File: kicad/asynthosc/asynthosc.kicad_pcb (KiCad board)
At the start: 4 copper layers, 69 x 106 mm, 218 parts, among them J1 USB_B_Micro, J10 AudioJack3, J11 AudioJack3, J12 RJ45_LED_Shielded, J13 AudioJack3, J14 AudioJack3, J2 Conn_02x05_Odd_Even, J3 Conn_ARM_SWD_TagConnect_TC203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, J4 Conn_02x07_Odd_Even, J5 Conn_02x04_Odd_Even, J6 AudioJack3, J7 AudioJack3, J8 AudioJack3, J9 AudioJack3, Q1 Q_NPN_BEC, Q2 Q_NPN_BEC, SW1 SW_Push, SW10 SW_MEC_5G_LED, SW11 SW_DIP_x04, SW2 SW_MEC_5G_LED, SW6 SW_MEC_5G_LED, SW8 RotaryEncoder, SW9 SW_MEC_5G_LED, U1 LM1117S-3.3, U10 LAN8742A, U11 USBLC6-2P6, U12 H11L1, U2 LMR62421XMF, U3 USBLC6-2SC6, U4 LM1117S-5.0, U5 Si1869DH, U6 STM32F723VETx, U7 W25Q32JVSS, U8 MCP6004, U9 MCP6004, Y1 8MHz, 8pF, Y2 25MHZ,20PF,30PPM

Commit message: pcb: place and change some components for easier routing
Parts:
- removed D10, D11, D12, D13, D14, D16, D17, D9: D_Schottky_1N5817, Diode_SMD:D_SOD-123
- removed SW11: SW_DIP_x04, Button_Switch_SMD:SW_DIP_SPSTx04_Slide_6.7x11.72mm_W8.61mm_P2.54mm_LowProfile
- removed TP1, TP4: TestPoint, TestPoint:TestPoint_Pad_D1.0mm
- added D22: D_Schottky_Dual_SD103ASDM, Package_TO_SOT_SMD:SOT-23-6, F.Cu at (99.1, 115.5)
- added D24: D_Schottky_Dual_SD103ASDM, Package_TO_SOT_SMD:SOT-23-6, F.Cu at (142.4, 116.3)
- added SW3: SW_DIP_x02, Button_Switch_SMD:SW_DIP_SPSTx02_Slide_9.78x7.26mm_W8.61mm_P2.54mm, F.Cu at (92.5, 134.0)
- added SW4: SW_DIP_x02, Button_Switch_SMD:SW_DIP_SPSTx02_Slide_9.78x7.26mm_W8.61mm_P2.54mm, F.Cu at (148.5, 134.0)
- moved R32 133.4 mm to (89.0, 119.1), turned to 180 degrees
- moved C34 132.3 mm to (88.5, 120.5), turned to 180 degrees
- moved R30 130.3 mm to (92.0, 122.0)
- moved R31 127.7 mm to (93.0, 122.0), turned to -90 degrees
- moved C31 100.3 mm to (118.5, 127.0), turned to 90 degrees
- moved R23 98.6 mm to (115.5, 133.0)
- moved R20 97.8 mm to (117.0, 130.5), turned to 180 degrees
- moved C32 97.8 mm to (118.0, 133.0), turned to 180 degrees
- moved R22 96.2 mm to (118.0, 131.5)
- moved R21 95.8 mm to (118.5, 130.0), turned to -90 degrees
- moved R37 84.1 mm to (94.0, 122.0), turned to -90 degrees
- moved R36 82.9 mm to (95.0, 122.0), turned to -90 degrees
- moved R38 81.9 mm to (97.0, 119.0)
- moved C35 80.2 mm to (97.5, 120.5)
- moved U9 65.0 mm to (148.0, 116.5), turned to 90 degrees
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- renumbered JP11 to JP10, JP4 to JP3, JP5 to JP4, JP6 to JP5, JP7 to JP6, JP8 to JP7, JP9 to JP8, JP10 to JP9, SW6 to SW5, SW8 to SW6, SW9 to SW7, SW10 to SW8
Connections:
- C32 pad 1: Net-(U9D-+) -> Net-(U8C-+)
- C33 pad 1: unconnected-(C33-Pad1) -> GND
- C36 pad 2: Net-(U8C--) -> Net-(U9A--)
- C37 pad 1: unconnected-(C37-Pad1) -> GND
- C50 pad 2: Net-(U8D--) -> Net-(U9B--)
- JP8 pad 1: Net-(JP9-A) -> Net-(JP8-A)
- R21 pad 1: Net-(U9D-+) -> Net-(U8C-+)
- R22 pad 2: Net-(U9D-+) -> Net-(U8C-+)
- R41 pad 1: Net-(U8C--) -> Net-(U9A--)
- R42 pad 1: Net-(U8C-+) -> Net-(U9A-+)
- R43 pad 1: Net-(U8C-+) -> Net-(U9A-+)
- R44 pad 2: Net-(U8C--) -> Net-(U9A--)
- R72 pad 1: Net-(U8D--) -> Net-(U9B--)
- R73 pad 1: Net-(U8D-+) -> Net-(U9B-+)
- R74 pad 1: Net-(U8D-+) -> Net-(U9B-+)
- R75 pad 2: Net-(U8D--) -> Net-(U9B--)
- U10 pad 15: Net-(JP9-A) -> Net-(JP8-A)
- U8 pad 12: Net-(U8D-+) -> (no net)
- U8 pad 13: Net-(U8D--) -> (no net)
- U8 pad 14: /Analog_in/CVIN3 -> (no net)
- U8 pad 8: /Analog_in/CVIN2 -> Net-(C32-Pad2)
- U8 pad 9: Net-(U8C--) -> GND
- U9 pad 1: (no net) -> /Analog_in/CVIN2
- U9 pad 12: Net-(U9D-+) -> (no net)
- U9 pad 13: GND -> (no net)
- U9 pad 14: Net-(C32-Pad2) -> (no net)
- U9 pad 2: (no net) -> Net-(U9A--)
- U9 pad 3: (no net) -> Net-(U9A-+)
- U9 pad 5: (no net) -> Net-(U9B-+)
- U9 pad 6: (no net) -> Net-(U9B--)
- U9 pad 7: (no net) -> /Analog_in/CVIN3

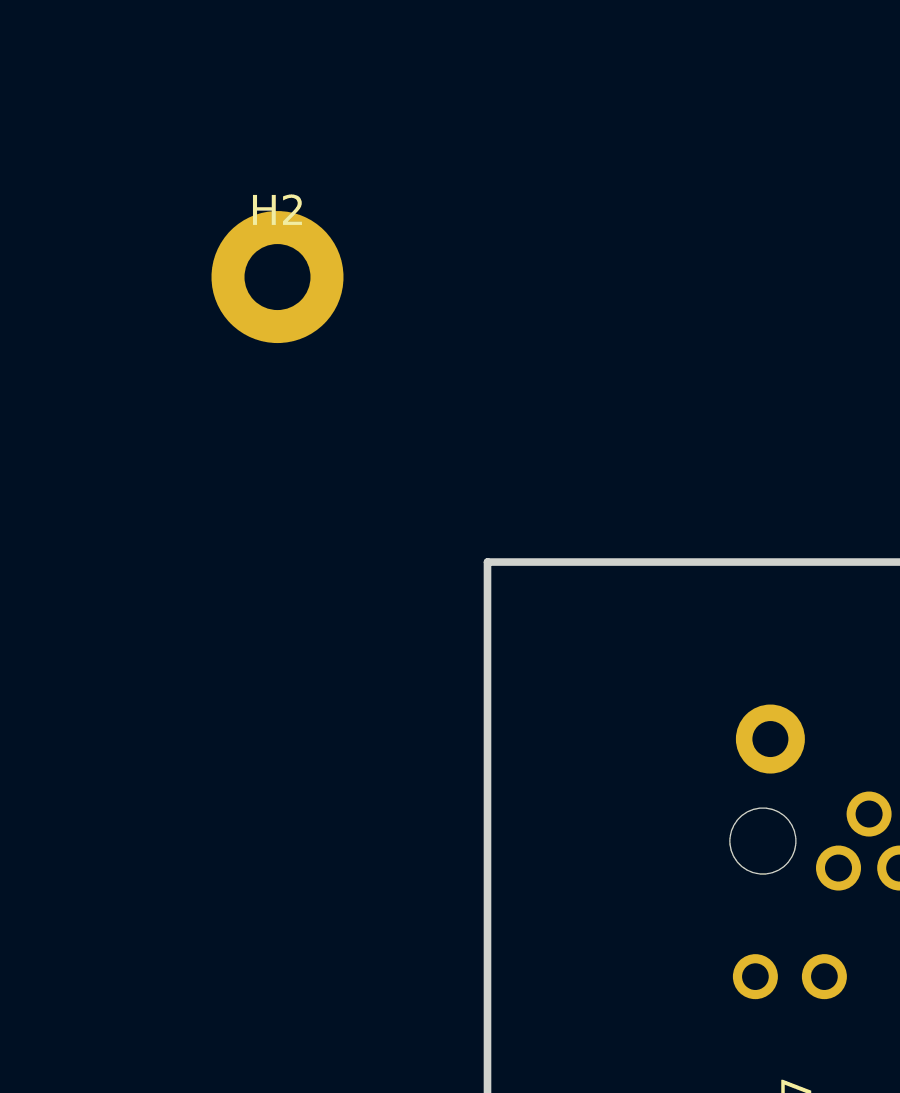
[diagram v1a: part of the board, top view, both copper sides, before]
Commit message: pcb: moving graphical elements
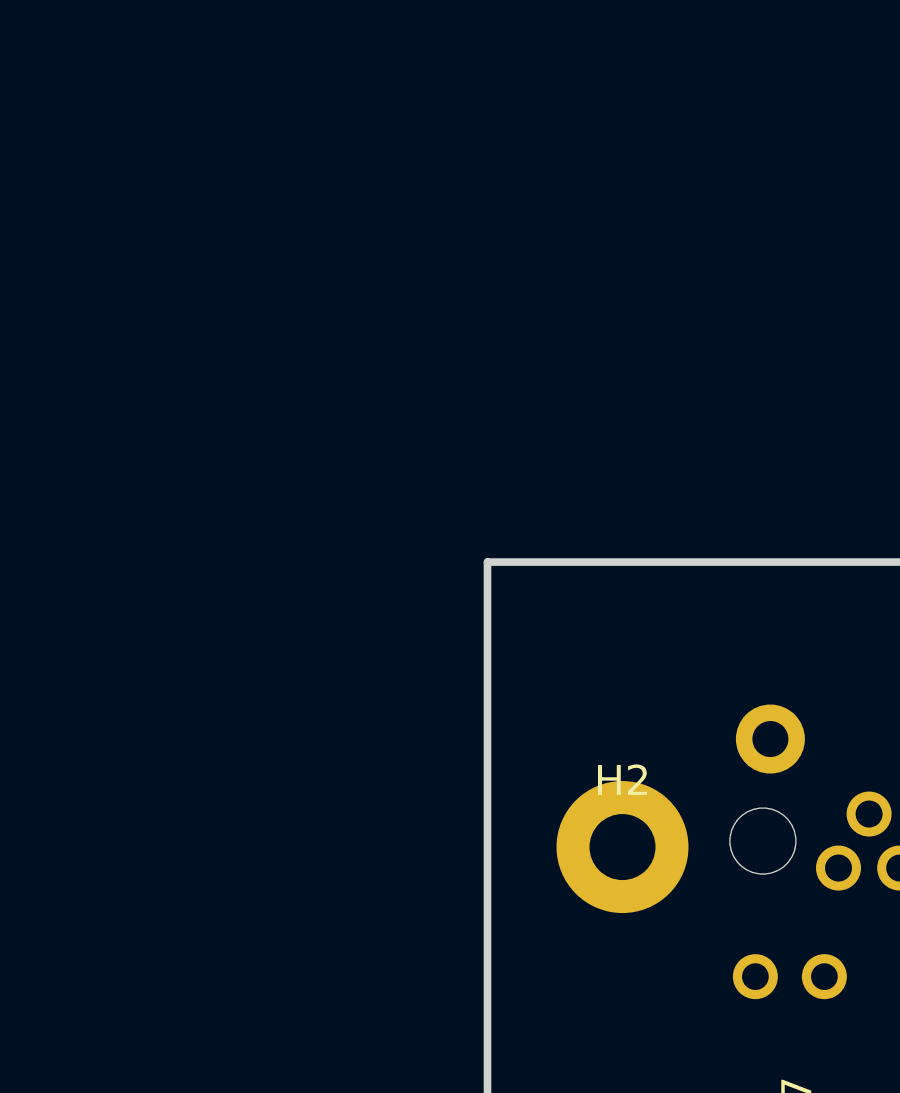
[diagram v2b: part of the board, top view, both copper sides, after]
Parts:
- moved H2 22.2 mm to (90.5, 53.5)
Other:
- board text added: "(opt) Eurorack PWR"
- board text added: "Jacks"
- board text added: "RJ45"
- board text added: "USB Micro-B"
- board text removed: "JACK"
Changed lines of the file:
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@@
 		(tags "SOT TO_SOT_SMD")
 		(property "Reference" "D22"
-			(at 0 -2.4 360)
+			(at 0 -2.4 0)
 			(layer "F.SilkS")
 			(effects
@@
 		)
 		(property "Value" "D_Schottky_Dual_SD103ASDM"
-			(at 0 2.4 360)
+			(at 0 2.4 0)
 			(layer "F.Fab")
 			(effects
@@
 		)
 		(fp_text user "${REFERENCE}"
-			(at 0 0 360)
+			(at 0 0 0)
 			(layer "F.Fab")
 			(effects
@@
 		(tags "capacitor electrolytic")
 		(property "Reference" "C3"
-			(at 0 -3.2 360)
+			(at 0 -3.2 0)
 			(layer "F.SilkS")
 			(effects
@@
 		)
 		(property "Value" "10uF"
-			(at 0 3.2 360)
+			(at 0 3.2 0)
 			(layer "F.Fab")
 			(effects
@@
 		)
 		(fp_text user "${REFERENCE}"
-			(at 0 0 360)
+			(at 0 0 0)
 			(layer "F.Fab")
 			(effects
@@
 		(tags "SOT TO_SOT_SMD")
 		(property "Reference" "D24"
-			(at 0 -2.4 360)
+			(at 0 -2.4 0)
 			(layer "F.SilkS")
 			(effects
@@
 		)
 		(property "Value" "D_Schottky_Dual_SD103ASDM"
-			(at 0 2.4 360)
+			(at 0 2.4 0)
 			(layer "F.Fab")
 			(effects
@@
 		)
 		(fp_text user "${REFERENCE}"
-			(at 0 0 360)
+			(at 0 0 0)
 			(layer "F.Fab")
 			(effects
@@
 	(footprint "MountingHole:MountingHole_2.2mm_M2_Pad"
 		(layer "F.Cu")
-		(at 79 34.5)
+		(at 90.5 53.5)
 		(descr "Mounting Hole 2.2mm, M2")
 		(tags "mounting hole 2.2mm m2")
@@
 	)
 	(gr_circle
+		(center 90 146)
+		(end 91.75 146)
+		(stroke
+			(width 0.2)
+			(type default)
+		)
+		(fill none)
+		(layer "Eco1.User")
+	)
+	(gr_circle
 		(center 148.62 158.6)
 		(end 150.37 158.6)
@@
 	)
 	(gr_rect
-		(start 133 116)
-		(end 144 126)
+		(start 131.5 115.5)
+		(end 142.5 125.5)
 		(stroke
 			(width 0.5)
@@
 	)
 	(gr_rect
-		(start 98.5 67)
-		(end 109.5 77)
+		(start 98.5 68)
+		(end 109.5 78)
 		(stroke
 			(width 0.5)
@@
 	)
 	(gr_circle
-		(center 127 143.4)
-		(end 131.9 143.4)
+		(center 126 142)
+		(end 130.9 142)
 		(stroke
 			(width 0.1)
@@
 	)
 	(gr_rect
-		(start 99.04 115.64)
-		(end 110.04 125.64)
+		(start 98.5 115.64)
+		(end 109.5 125.64)
 		(stroke
 			(width 0.5)
@@
 	)
 	(gr_circle
-		(center 116.2 131.3)
-		(end 121.1 131.3)
+		(center 115 130)
+		(end 119.9 130)
 		(stroke
 			(width 0.1)
@@
 	)
 	(gr_circle
-		(center 104.5 142.8)
-		(end 109.4 142.8)
+		(center 104 142)
+		(end 108.9 142)
 		(stroke
 			(width 0.1)
@@
 	)
 	(gr_circle
-		(center 127 131.2)
-		(end 131.9 131.2)
+		(center 126 130)
+		(end 130.9 130)
 		(stroke
 			(width 0.1)
@@
 	)
 	(gr_circle
-		(center 138 143.1)
-		(end 142.9 143.1)
+		(center 137 142)
+		(end 141.9 142)
 		(stroke
 			(width 0.1)
@@
 	)
 	(gr_circle
-		(center 115.9 143.4)
-		(end 120.8 143.4)
+		(center 115 142)
+		(end 119.9 142)
 		(stroke
 			(width 0.1)
@@
 		(layer "Eco1.User")
 	)
+	(gr_circle
+		(center 90.5 53.5)
+		(end 92.25 53.5)
+		(stroke
+			(width 0.2)
+			(type default)
+		)
+		(fill none)
+		(layer "Eco1.User")
+	)
 	(gr_rect
-		(start 131.5 67)
-		(end 142.5 77)
+		(start 131.5 68)
+		(end 142.5 78)
 		(stroke
 			(width 0.5)
@@
 	)
 	(gr_circle
-		(center 104.8 130.9)
-		(end 109.7 130.9)
+		(center 104 130)
+		(end 108.9 130)
 		(stroke
 			(width 0.1)
@@
 	)
 	(gr_circle
-		(center 138.2 131.3)
-		(end 143.1 131.3)
+		(center 137 130)
+		(end 141.9 130)
 		(stroke
 			(width 0.1)
@@
 	)
 	(gr_circle
-		(center 120.4 72.8)
-		(end 126.45 72.8)
+		(center 151 146)
+		(end 152.75 146)
+		(stroke
+			(width 0.2)
+			(type default)
+		)
+		(fill none)
+		(layer "Eco1.User")
+	)
+	(gr_circle
+		(center 120.5 73)
+		(end 126.55 73)
 		(stroke
 			(width 0.5)
@@
 		)
 	)
-	(gr_text "JACK"
-		(at 102.5 140.7 0)
+	(gr_text "AUDIO OUT\n"
+		(at 111.5 131 0)
 		(layer "Eco1.User")
 		(effects
@@
 		)
 	)
-	(gr_text "AUDIO OUT\n"
-		(at 121.9 131.2 0)
-		(layer "Eco1.User")
+	(gr_text "RJ45\n"
+		(at 103.5 43.5 0)
+		(layer "Eco1.User" knockout)
 		(effects
 			(font
@@
 				(thickness 0.15)
 			)
-			(justify left bottom)
+			(justify left bottom mirror)
+		)
+	)
+	(gr_text "Jacks"
+		(at 147.5 130.5 0)
+		(layer "Eco1.User" knockout)
+		(effects
+			(font
+				(size 1 1)
+				(thickness 0.15)
+			)
+			(justify left bottom mirror)
 		)
 	)
@@
 		)
 	)
+	(gr_text "(opt) Eurorack PWR"
+		(at 147.5 43.5 0)
+		(layer "Eco1.User" knockout)
+		(effects
+			(font
+				(size 1 1)
+				(thickness 0.15)
+			)
+			(justify left bottom mirror)
+		)
+	)
 	(gr_text "DISPLAY\n"
-		(at 117.5 53.5 0)
+		(at 117.5 53.5 -0)
 		(layer "Eco1.User")
 		(effects
@@
 	)
 	(gr_text "BTN"
-		(at 138.5 72 -0)
+		(at 135.5 72 -0)
 		(layer "Eco1.User")
 		(effects
@@
 	)
 	(gr_text "(cancel)"
-		(at 135.4 73.4 0)
+		(at 134 74 0)
 		(layer "Eco1.User")
 		(effects
@@
 	)
 	(gr_text "MIDI IN"
-		(at 112.5 131.8 0)
+		(at 123.5 131 -0)
 		(layer "Eco1.User")
 		(effects
@@
 		)
 	)
+	(gr_text "USB Micro-B"
+		(at 121.5 43.5 0)
+		(layer "Eco1.User" knockout)
+		(effects
+			(font
+				(size 1 1)
+				(thickness 0.15)
+			)
+			(justify left bottom mirror)
+		)
+	)
 	(gr_text "Between boards: 13mm interval"
 		(at 107.5 20 0)
@@
 	)
 	(gr_text "(OK)"
-		(at 102.6 71.8 0)
+		(at 102 73.5 0)
 		(layer "Eco1.User")
 		(effects
@@
 	)
 	(gr_text "RJ45 height: 11.7mm"
-		(at 89.6 43 0)
+		(at 93 41.5 0)
 		(layer "Eco1.User")
 		(effects
@@
 		)
 		(height -42.084344)
-		(gr_text "106,0000 mm"
+		(gr_text "106.0000 mm"
 			(at 45.106919 97.031859 -89.9554066)
 			(layer "Dwgs.User")
@@
 		)
 		(height -6.3)
-		(gr_text "69,0000 mm"
+		(gr_text "69.0000 mm"
 			(at 120.5 155.15 0)
 			(layer "Dwgs.User")
@@
 		)
 		(height 6.199999)
-		(gr_text "7,5000 mm"
+		(gr_text "7.5000 mm"
 			(at 88.75 28.850001 0)
 			(layer "Eco1.User")
@@
 		)
 		(height -9)
-		(gr_text "71,1200 mm"
+		(gr_text "71.1200 mm"
 			(at 120.56 23.05 0)
 			(layer "Eco1.User")
@@
 		)
 		(height 4.93)
-		(gr_text "3,0000 mm"
+		(gr_text "3.0000 mm"
 			(at 99.4 34.705 90)
 			(layer "Eco1.User")
@@
 		)
 		(height 30.2)
-		(gr_text "128,4000 mm"
+		(gr_text "128.4000 mm"
 			(at 53.65 97.4 90)
 			(layer "Eco1.User")

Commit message: wip: place
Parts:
- moved R34 7.64 mm to (98.0, 137.0)
- moved R33 4.15 mm to (97.5, 138.8), turned to -90 degrees
- moved R28 4.08 mm to (87.5, 140.2)
- moved R27 2.14 mm to (91.2, 141.0), turned to 90 degrees
- moved D24 1.07 mm to (142.5, 115.2)
- moved D22 0.92 mm to (98.2, 115.2)
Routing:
- net Net-(SW3B-1): track 0.00 -> 27.8 mm
- net Net-(SW3B-2): track 0.00 -> 10.1 mm

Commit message: pcb: place and draft route
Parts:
- added U13: USBLC6-2P6, Package_TO_SOT_SMD:SOT-666, F.Cu at (103.2, 92.2)
- moved R20 30.2 mm to (94.0, 111.0), turned to -90 degrees
- moved R21 30.0 mm to (95.2, 111.0), turned to 90 degrees
- moved R22 29.3 mm to (95.2, 113.0), turned to 90 degrees
- moved C32 29.2 mm to (96.8, 113.0), turned to -90 degrees
- moved C31 26.7 mm to (97.8, 110.2), turned to 0 degrees
- moved R23 25.6 mm to (97.0, 115.2), turned to 180 degrees
- moved C44 24.2 mm to (109.2, 80.8), turned to 180 degrees
- moved C45 21.1 mm to (109.2, 84.0), turned to 0 degrees
- moved U11 17.1 mm to (90.0, 92.2), turned to 180 degrees
- moved C11 16.2 mm to (129.8, 51.8), turned to 180 degrees
- moved R64 15.9 mm to (90.7, 75.2)
- moved R65 14.7 mm to (89.5, 75.2), turned to 90 degrees
- moved C10 14.5 mm to (129.8, 50.8)
- moved C48 14.2 mm to (94.7, 75.7)
- moved FB1 13.8 mm to (131.5, 51.2), turned to -90 degrees
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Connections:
- U11 pad 3: /Soc/Ethernet/TX_P -> /Soc/Ethernet/RX_N
- U11 pad 4: /Soc/Ethernet/TX_N -> /Soc/Ethernet/RX_N
- U11 pad 6: /Soc/Ethernet/RX_N -> /Soc/Ethernet/RX_P
- U6 pad 81: /Soc/UART4_RX -> /Midi_in/MIDI_TO_SOC
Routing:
- net /Analog_in/CVIN0: track 0.00 -> 70.5 mm
- net /Analog_in/CVIN1: track 0.00 -> 69.1 mm
- net /Soc/DAC_OUT1: track 0.00 -> 51.3 mm
- net /Soc/USB_ID: track 0.00 -> 48.5 mm, vias 0 -> 1
- net /Soc/Ethernet/RJ45_LED2: track 0.00 -> 44.6 mm
- net /Soc/Ethernet/RJ45_LED1: track 0.00 -> 43.5 mm
- net /Soc/USB_D_N: track 0.00 -> 41.8 mm
- net /Analog_in/CVIN3: track 0.00 -> 40.3 mm
- net /Soc/USB_D_P: track 0.00 -> 38.7 mm
- net /Analog_in/CVIN2: track 0.00 -> 37.5 mm
- net Net-(J6-PadT): track 0.00 -> 37.4 mm
- net /Soc/Ethernet/RJ_TX_P: track 0.00 -> 34.7 mm, vias 0 -> 1
- net /Soc/Ethernet/RJ_RX_P: track 0.00 -> 34.2 mm, vias 0 -> 1
- net /Soc/Ethernet/RJ_TX_N: track 0.00 -> 33.6 mm, vias 0 -> 1
- net GND: track 0.00 -> 31.4 mm, vias 0 -> 4
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- added copper zone on F.Cu, net /Supply/VBUS
- added copper zone on In1.Cu, net GND

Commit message: pcb: routing wip
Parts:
- C5, C8, C9, D2, D5, U4: moved to F.Cu
- moved C9 38.8 mm to (145.0, 66.0), turned to -90 degrees
- moved R8 30.9 mm to (148.4, 80.3)
- moved D5 29.3 mm to (145.0, 60.5), turned to -90 degrees
- moved U4 27.2 mm to (150.8, 59.8), turned to -90 degrees
- moved C8 26.5 mm to (152.5, 52.5), turned to 0 degrees
- moved C3 20.3 mm to (139.0, 84.2), turned to 180 degrees
- moved C7 16.2 mm to (143.7, 68.6), turned to 180 degrees
- moved L1 12.3 mm to (147.6, 86.2), turned to 0 degrees
- moved D2 10.8 mm to (148.5, 45.5), turned to 180 degrees
- moved D4 10.3 mm to (147.2, 71.5), turned to -90 degrees
- moved C5 9.44 mm to (151.0, 49.0)
- moved R3 9.22 mm to (144.8, 74.2), turned to 90 degrees
- moved R4 9.15 mm to (143.8, 76.1), turned to 90 degrees
- moved C6 7.83 mm to (144.8, 76.1), turned to -90 degrees
- moved JP2 6.17 mm to (142.2, 52.6)
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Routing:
- net 5V: track 10.2 -> 153.7 mm, vias 0 -> 6
- net +10V: track 0.00 -> 73.9 mm, vias 0 -> 16
- net 3V3: track 0.00 -> 56.7 mm, vias 0 -> 12
- net /Supply/DISP_12V_EN: track 0.00 -> 56.0 mm
- net /Interface/SCLK: track 0.00 -> 40.9 mm
- net /Interface/DC: track 0.00 -> 39.6 mm
- net /Interface/SDIN: track 0.00 -> 38.8 mm
- net /Interface/nCS: track 0.00 -> 36.8 mm
- net /Interface/nRST: track 0.00 -> 36.6 mm
- net Net-(U6-PA9): track 0.00 -> 21.6 mm
- net /Supply/IN_+12V: track 0.00 -> 21.1 mm
- net /Supply/5V_EUR: track 0.00 -> 11.2 mm
- net Net-(DS1-IREF): track 0.00 -> 5.81 mm, vias 0 -> 1
- net Net-(DS1-VCOMH): track 0.00 -> 4.68 mm, vias 0 -> 1
- net /Supply/EUR_+12V: track 0.00 -> 3.76 mm
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- added copper zone on In2.Cu, net /Supply/VBUS
- added copper zone on In2.Cu, net 3V3
- added copper zone on In2.Cu, net GND

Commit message: pcb: route
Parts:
- moved J3 61.4 mm to (140.5, 104.0), turned to 180 degrees
- moved J4 57.4 mm to (148.8, 106.0), turned to 0 degrees
- moved R8 9.48 mm to (139.0, 81.0), turned to 180 degrees
- moved J5 8.25 mm to (147.2, 90.5)
- moved R2 2.23 mm to (144.8, 79.2), turned to 90 degrees
- moved C9 1.49 mm to (143.6, 65.5), turned to 180 degrees
- moved C8 1.12 mm to (151.5, 53.0)
- moved R30 1.00 mm to (92.5, 123.7)
- moved R31 1.00 mm to (91.5, 123.8)
- moved R36 1.00 mm to (93.5, 123.8)
- moved R37 0.99 mm to (94.5, 123.8)
- moved R28 0.56 mm to (88.0, 135.8), turned to 90 degrees
- moved R34 0.56 mm to (98.0, 135.8), turned to 90 degrees
- moved R40 0.56 mm to (143.0, 135.2), turned to 90 degrees
- moved R71 0.56 mm to (153.0, 135.2), turned to 90 degrees
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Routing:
- net /Soc/JTCK_CONN: track 0.00 -> 60.4 mm, vias 0 -> 2
- net /Soc/JTMS_CONN: track 0.00 -> 58.5 mm, vias 0 -> 2
- net /Soc/JTDO_CONN: track 0.00 -> 46.2 mm, vias 0 -> 2
- net /Soc/JTDI_CONN: track 0.00 -> 44.8 mm, vias 0 -> 1
- net /Soc/NRST_CONN: track 0.00 -> 44.8 mm, vias 0 -> 3
- net /Soc/QSPI_BK2_IO2: track 0.00 -> 32.6 mm, vias 0 -> 2
- net /Soc/QSPI_BK2_IO3: track 0.00 -> 28.4 mm, vias 0 -> 2
- net /Soc/QSPI_CLK: track 0.00 -> 14.5 mm, vias 0 -> 1
- net Net-(D4-A): track 2.82 -> 13.8 mm
- net /Supply/VBUS: track 4.26 -> 14.8 mm
- net Net-(U6-PA9): track 21.6 -> 11.2 mm
- net /Soc/NRST: track 0.00 -> 6.86 mm
- net /Soc/QSPI_BK2_IO1: track 0.00 -> 6.64 mm, vias 0 -> 1
- net /Soc/QSPI_BK2_NCS: track 0.00 -> 6.62 mm, vias 0 -> 1
- net 5V: track 153.7 -> 160.1 mm, vias 6 -> 12
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
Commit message: pcb: routing
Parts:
- removed the JP9 at (102.4, 99.1)
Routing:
- net /Soc/RMII_TXD1: track 0.00 -> 42.4 mm, vias 0 -> 2
- net /Soc/RMII_RXD1: track 0.00 -> 39.0 mm, vias 0 -> 2
- net /Soc/RMII_RXD0: track 0.00 -> 34.5 mm, vias 0 -> 2
- net /Soc/RMII_TXD0: track 0.00 -> 33.3 mm, vias 0 -> 2
- net /Soc/RMII_MDIO: track 0.00 -> 32.3 mm, vias 0 -> 2
- net /Soc/RMII_TX_EN: track 0.00 -> 31.9 mm, vias 0 -> 2
- net /Soc/RMII_CRS_DV: track 0.00 -> 29.6 mm, vias 0 -> 2
- net /Soc/RMII_REF_CLK: track 0.00 -> 26.9 mm, vias 0 -> 2
- net /Soc/RMII_MDC: track 0.15 -> 26.3 mm, vias 0 -> 2
- net Net-(U10-~{INT}/REFCLKO): track 0.00 -> 2.36 mm
- net Net-(JP8-A): track 0.00 -> 2.20 mm

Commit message: pcb: routing
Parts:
- removed the JP3 at (133.8, 104.5)
- moved C25 9.22 mm to (110.5, 105.0), turned to 180 degrees
- moved R80 5.56 mm to (104.5, 68.5), turned to 180 degrees
- moved R81 5.54 mm to (136.5, 68.5)
- moved J4 4.50 mm to (148.8, 110.5)
- moved R17 4.11 mm to (104.5, 98.0), turned to 180 degrees
- moved C18 4.10 mm to (104.5, 99.0), turned to 0 degrees
- moved R78 1.75 mm to (109.0, 75.5), turned to 180 degrees
- moved R79 1.52 mm to (131.8, 75.5)
- moved C30 1.05 mm to (142.7, 96.8), turned to 0 degrees
- moved J5 1.03 mm to (147.2, 89.5), turned to 90 degrees
- moved R11 1.00 mm to (110.5, 96.0)
- moved R12 1.00 mm to (110.5, 95.0)
- moved JP4 0.77 mm to (120.7, 107.0), turned to -90 degrees
- moved C23 0.77 mm to (118.3, 112.2)
- moved C24 0.77 mm to (121.8, 112.2)
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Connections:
- R5 pad 2: /Supply/DISP_12V_EN -> /Soc/DISP_12V_EN
- U5 pad 5: /Supply/DISP_12V_EN -> /Soc/DISP_12V_EN
- U6 pad 43: /Analog_in/TRG1 -> /Analog_in/TRG0
- U6 pad 44: unconnected-(U6-PE14-Pad44) -> /Analog_in/TRG1
- U6 pad 56: unconnected-(U6-PB14-Pad56) -> /Soc/DISP_10V_EN
- U6 pad 57: unconnected-(U6-PB15-Pad57) -> /Soc/DISP_12V_EN
- U6 pad 58: unconnected-(U6-PD11-Pad58) -> /Interface/LED_BTN_2
- U6 pad 59: unconnected-(U6-PD12-Pad59) -> /Interface/BTN_2
- U6 pad 62: unconnected-(U6-PD15-Pad62) -> /Interface/DC
- U6 pad 63: unconnected-(U6-PC6-Pad63) -> /Interface/nRST
- U6 pad 64: unconnected-(U6-PC7-Pad64) -> /Interface/nCS
- U6 pad 65: unconnected-(U6-PC8-Pad65) -> /Interface/ROT_A
- U6 pad 66: unconnected-(U6-PC9-Pad66) -> /Interface/ROT_B
- U6 pad 83: unconnected-(U6-PD2-Pad83) -> /Interface/BTN_1
- U6 pad 84: unconnected-(U6-PD3-Pad84) -> /Interface/LED_BTN_1
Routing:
- net /Analog_in/TRG1: track 0.00 -> 86.7 mm, vias 0 -> 1
- net /Soc/DISP_12V_EN: track 0.00 -> 60.1 mm
- net /Supply/DISP_12V_EN: track 56.0 -> 0.00 mm
- net /Analog_in/TRG0: track 0.00 -> 54.7 mm, vias 0 -> 1
- net Net-(J5-Pin_7): track 0.00 -> 54.6 mm, vias 0 -> 2
- net Net-(J5-Pin_1): track 0.00 -> 53.2 mm, vias 0 -> 1
- net /Midi_in/MIDI_TO_SOC: track 0.22 -> 47.2 mm, vias 0 -> 2
- net /Soc/DISP_10V_EN: track 0.00 -> 30.5 mm
- net /Interface/LED_BTN_1: track 0.00 -> 27.9 mm, vias 0 -> 1
- net /Interface/BTN_1: track 0.00 -> 26.6 mm, vias 0 -> 1
- net Net-(J5-Pin_2): track 0.00 -> 26.2 mm, vias 0 -> 1
- net Net-(J10-PadT): track 0.00 -> 26.1 mm
- net Net-(SW3B-1): track 3.81 -> 29.9 mm
- net /Soc/NRST: track 6.96 -> 31.6 mm, vias 0 -> 2
- net /Interface/LED_BTN_2: track 0.00 -> 22.0 mm, vias 0 -> 1
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- added copper zone on F.Cu, net 3V3
- added copper zone on In2.Cu, net 3V3_FILT
